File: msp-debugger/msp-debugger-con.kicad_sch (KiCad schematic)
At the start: 12 parts, among them J1 USB_B_Mini, J2 Conn_02x10, SW1 SW_MEC_5E, SW2 SW_MEC_5E, SW3 SW_MEC_5E, SW4 SW_MEC_5E, U1 ESP32-WROOM-32, U2 NHD-0420H1Z

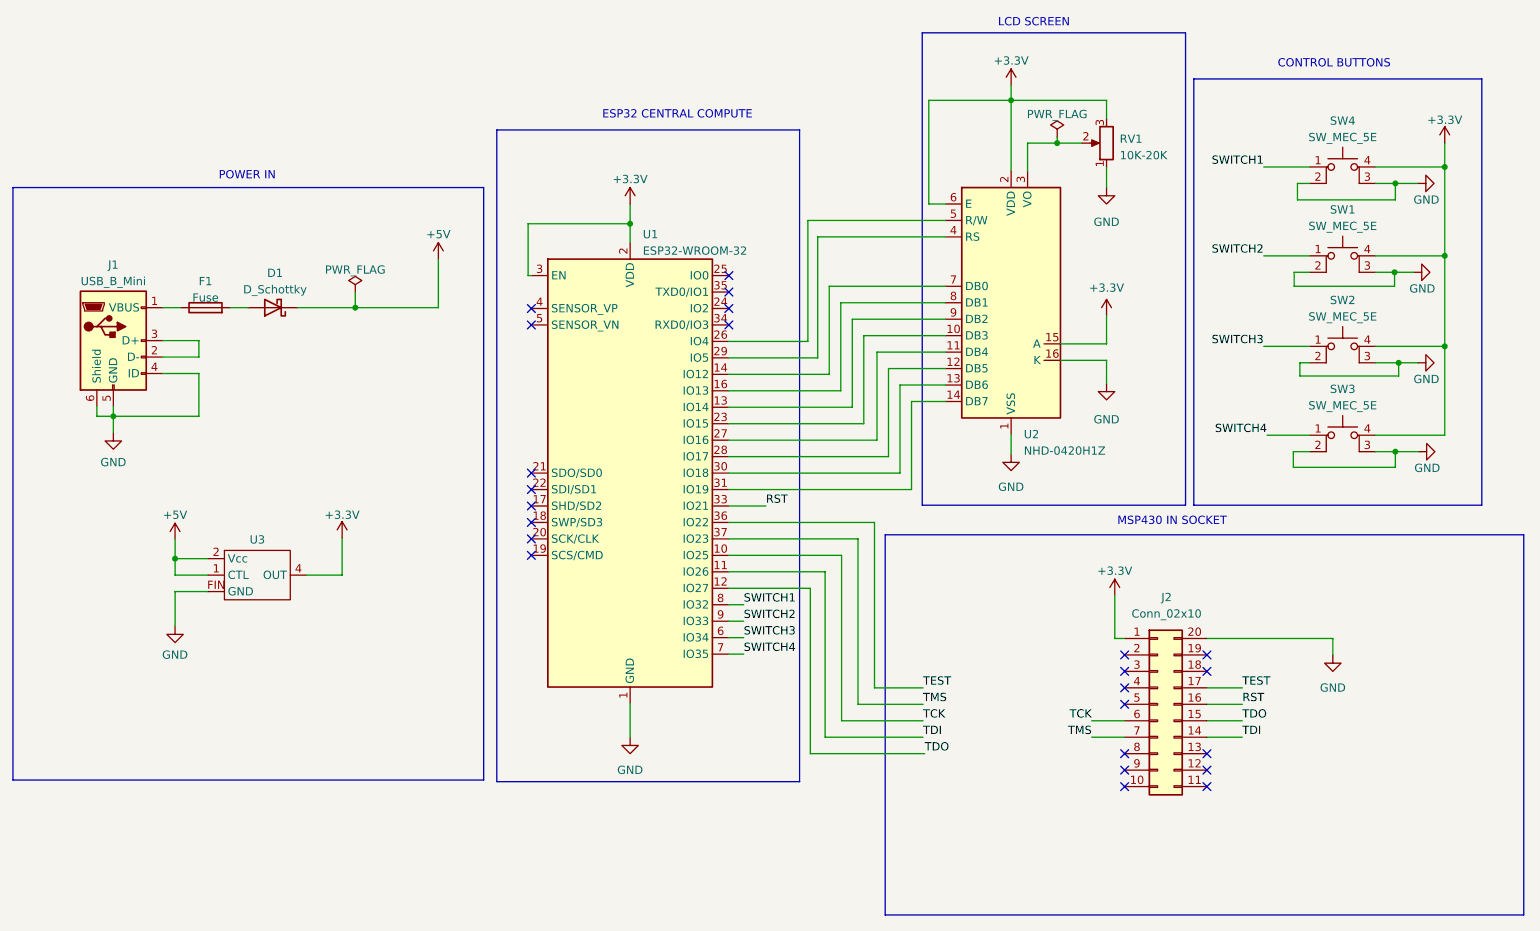
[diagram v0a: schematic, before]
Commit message: switch voltage divider for regulator
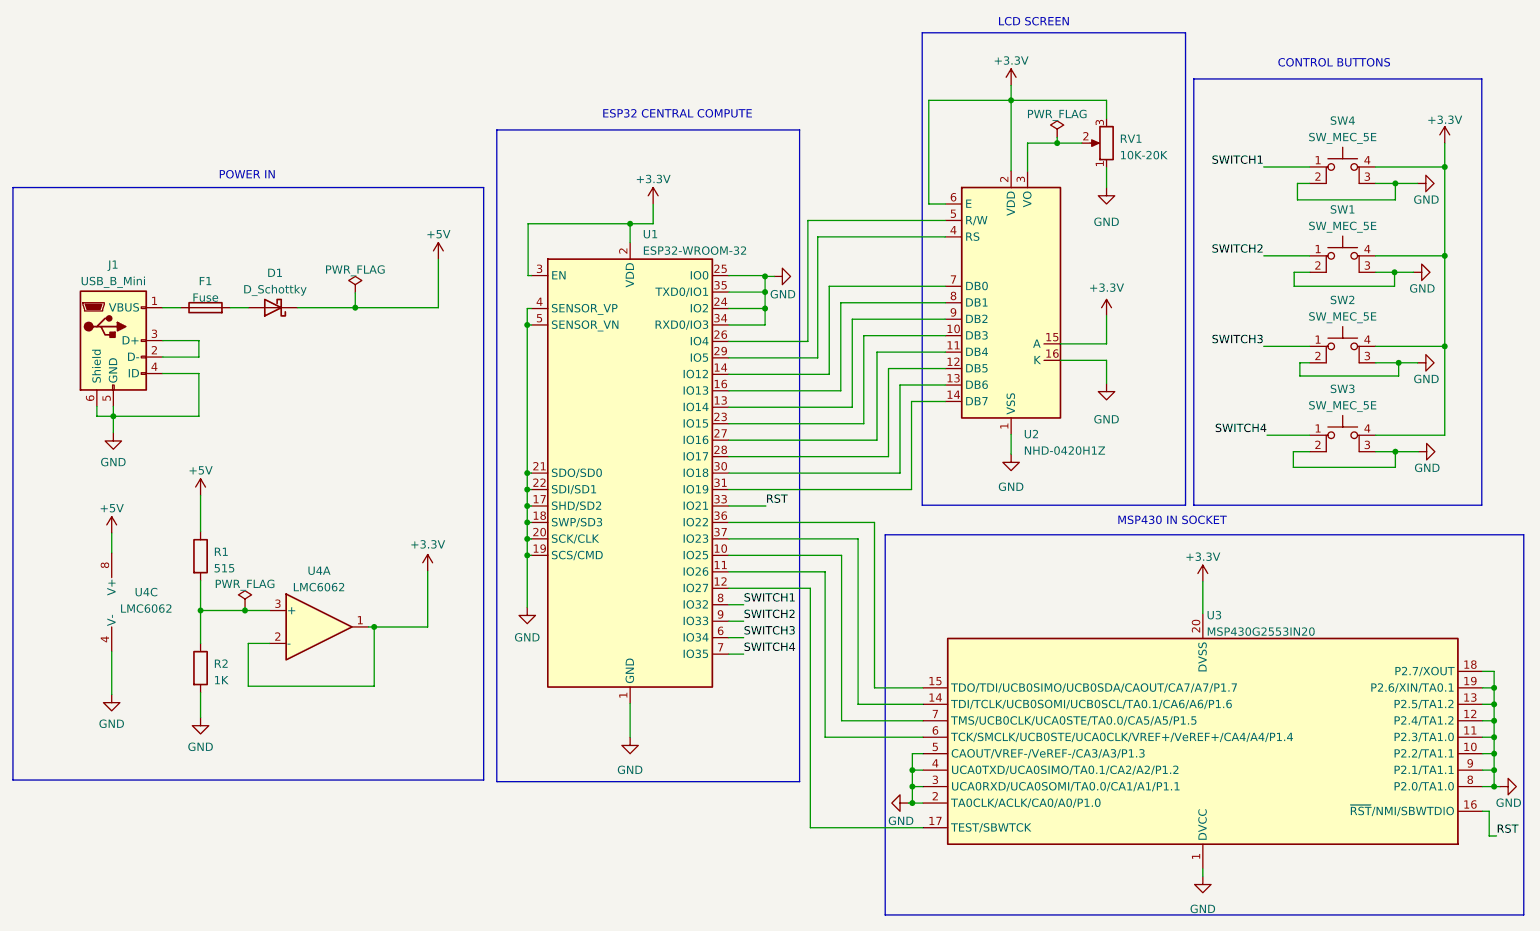
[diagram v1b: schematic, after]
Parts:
- removed J2: Conn_02x10, symbol Connector_Generic:Conn_02x10_Counter_Clockwise
- removed U3: ~, symbol ICs:BA033CC0FP-E2
- added R1: 515, symbol Device:R
- added R2: 1K, symbol Device:R
- added U3: MSP430G2553IN20, Package_DIP:DIP-20_W7.62mm, symbol MCU_Texas_MSP430:MSP430G2553IN20
- added U4: LMC6062, symbol Amplifier_Operational:LMC6062
- D1: footprint Diode_SMD:D_SOD-128 -> (none)
- F1: footprint Fuse:Fuse_1812_4532Metric -> (none)
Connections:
- net +3.3V: now also U3.20 (DVSS), U4.1, U4.2 (-)
- net +5V: now also R1.1, U4.8 (V+)
- net GND: now also U1.17 (SHD/SD2), U1.18 (SWP/SD3), U1.19 (SCS/CMD), U1.20 (SCK/CLK), U1.21 (SDO/SD0), U1.22 (SDI/SD1), U1.24 (IO2), U1.25 (IO0), U1.34 (RXD0/IO3), U1.35 (TXD0/IO1), U1.4 (SENSOR_VP), U1.5 (SENSOR_VN), R2.2, U3.1 (DVCC), U3.10 (P2.2/TA1.1), U3.11 (P2.3/TA1.0), U3.12 (P2.4/TA1.2), U3.13 (P2.5/TA1.2), U3.18 (P2.7/XOUT), U3.19 (P2.6/XIN/TA0.1), U3.2 (TA0CLK/ACLK/CA0/A0/P1.0), U3.3 (UCA0RXD/UCA0SOMI/TA0.0/CA1/A1/P1.1), U3.4 (UCA0TXD/UCA0SIMO/TA0.1/CA2/A2/P1.2), U3.5 (CAOUT/VREF-/VeREF-/CA3/A3/P1.3), U3.8 (P2.0/TA1.0), U3.9 (P2.1/TA1.1), U4.4 (V-)
- net RST: now also U3.16 (~{RST}/NMI/SBWTDIO)
- net TCK: no longer names the net of U1.10 (IO25)
- net TCK: now also U3.7 (TMS/UCB0CLK/UCA0STE/TA0.0/CA5/A5/P1.5)
- net TDI: no longer names the net of U1.11 (IO26)
- net TDI: now also U3.6 (TCK/SMCLK/UCB0STE/UCA0CLK/VREF+/VeREF+/CA4/A4/P1.4)
- net TDO: no longer names the net of U1.12 (IO27)
- net TDO: now also U3.17 (TEST/SBWTCK)
- net TEST: no longer names the net of U1.36 (IO22)
- net TEST: now also U3.15 (TDO/TDI/UCB0SIMO/UCB0SDA/CAOUT/CA7/A7/P1.7)
- net TMS: no longer names the net of U1.37 (IO23)
- net TMS: now also U3.14 (TDI/TCLK/UCB0SOMI/UCB0SCL/TA0.1/CA6/A6/P1.6)
- new net: R1.2, R2.1, U4.3 (+)
- no-connect marks 24 -> 0
